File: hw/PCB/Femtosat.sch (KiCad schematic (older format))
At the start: 6 parts, among them U1 SAMD21G, U2 TRH-G2, U5 XA1110, Y1 32.768kHz

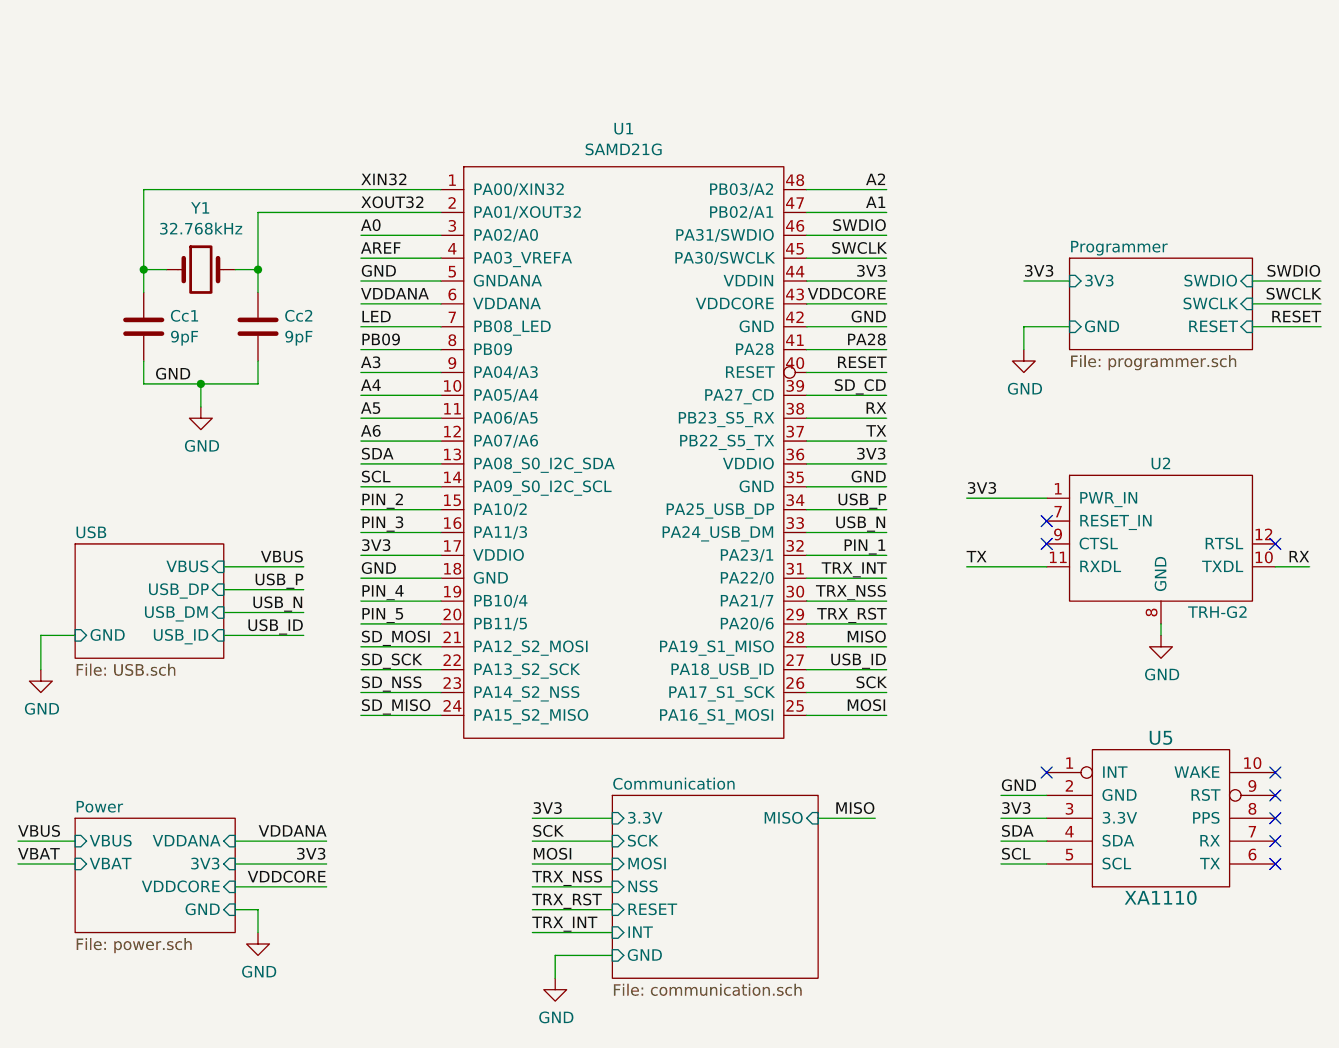
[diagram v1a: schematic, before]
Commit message: Added a footprint library for a micro SD card. Updated the schematic. Replaced the SAMD21G with the SAMD21E (32 pin variant). Added a data logger and a reset button.
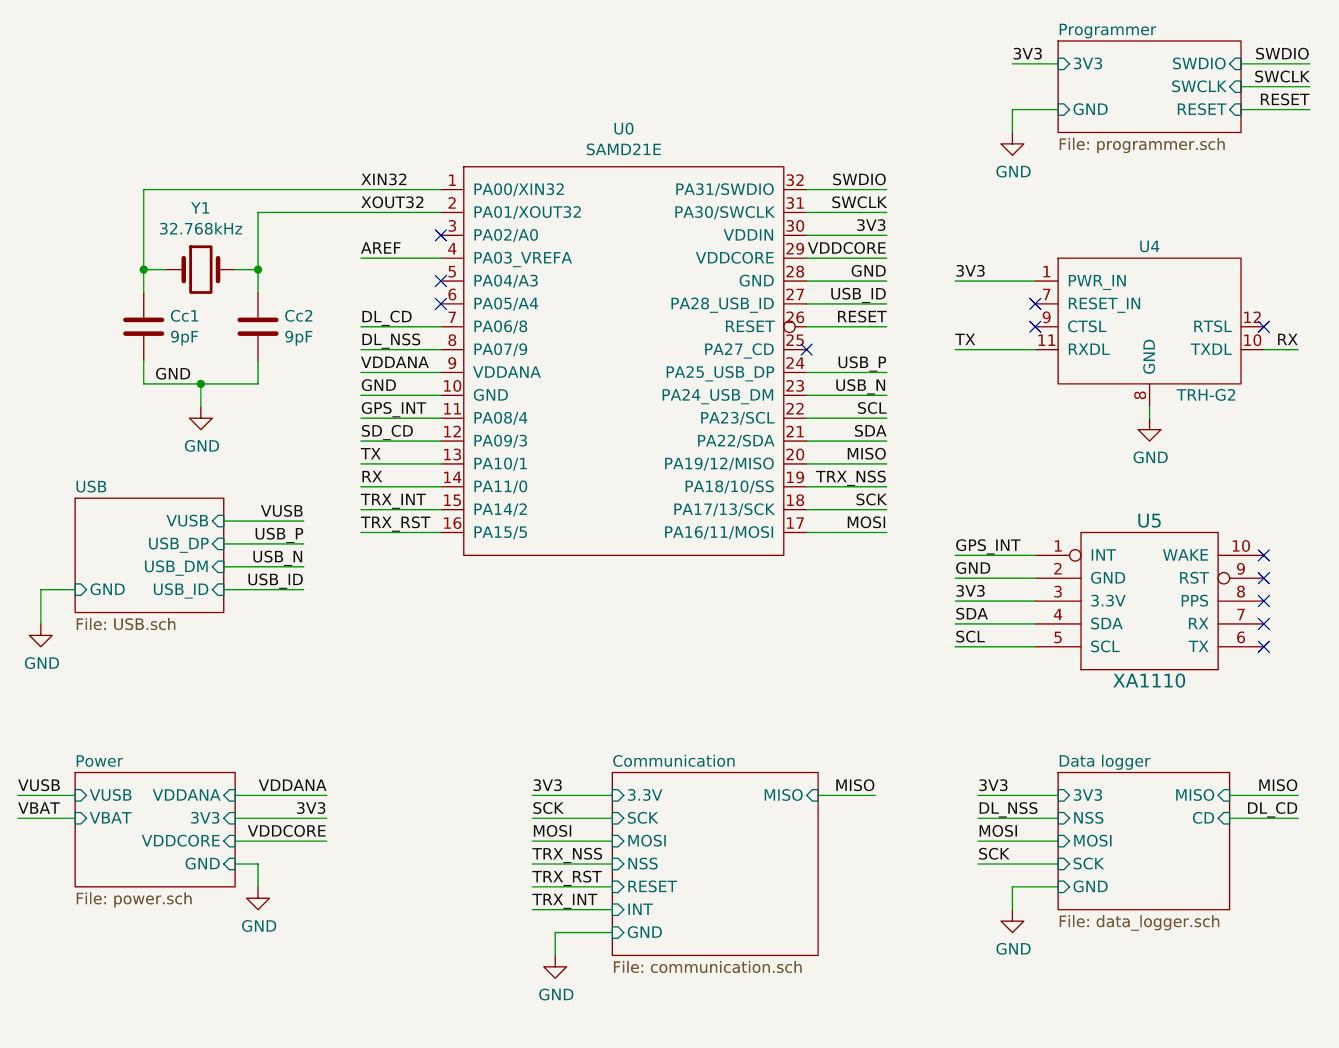
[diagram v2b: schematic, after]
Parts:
- removed U1: SAMD21G, Package_QFP:TQFP-48_7x7mm_P0.5mm, symbol Arduino:SAMD21G
- added U0: SAMD21E, symbol Arduino:SAMD21E
- renumbered U2 to U4
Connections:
- net 3V3: now also U0.30 (VDDIN)
- net AREF: now also U0.4 (PA03_VREFA)
- net GND: now also U0.10 (GND), U0.28 (GND)
- net MISO: now also U0.20 (PA19/12/MISO)
- net MOSI: now also U0.17 (PA16/11/MOSI)
- net RESET: now also U0.26 (RESET)
- net RX: now also U0.14 (PA11/0)
- net SCK: now also U0.18 (PA17/13/SCK)
- net SCL: now also U0.22 (PA23/SCL)
- net SDA: now also U0.21 (PA22/SDA)
- net SD_CD: now also U0.12 (PA09/3)
- net SWCLK: now also U0.31 (PA30/SWCLK)
- net SWDIO: now also U0.32 (PA31/SWDIO)
- net TRX_INT: now also U0.15 (PA14/2)
- net TRX_NSS: now also U0.19 (PA18/10/SS)
- net TRX_RST: now also U0.16 (PA15/5)
- net TX: now also U0.13 (PA10/1)
- net USB_ID: now also U0.27 (PA28_USB_ID)
- net USB_N: now also U0.23 (PA24_USB_DM)
- net USB_P: now also U0.24 (PA25_USB_DP)
- net VDDANA: now also U0.9 (VDDANA)
- net VDDCORE: now also U0.29 (VDDCORE)
- net XIN32: now also U0.1 (PA00/XIN32)
- net XOUT32: now also U0.2 (PA01/XOUT32)
- net GPS_INT: now reaches U5.1 (INT)
- net GPS_INT: now also U0.11 (PA08/4)
- new net DL_CD: U0.7 (PA06/8)
- new net DL_NSS: U0.8 (PA07/9)
- no-connect marks 9 -> 12
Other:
- moved on the sheet: U4, U5

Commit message: Added pullup resistor to the chip-select pin of the uSD card slot.
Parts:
- U0: footprint (none) -> Package_QFP:TQFP-32_7x7mm_P0.8mm
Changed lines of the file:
@@
 F 0 "U0" H 5200 3565 50  0000 C CNN
 F 1 "SAMD21E" H 5200 3474 50  0000 C CNN
-F 2 "" H 5200 2450 50  0001 C CNN
+F 2 "Package_QFP:TQFP-32_7x7mm_P0.8mm" H 5200 2450 50  0001 C CNN
 F 3 "" H 5200 2450 50  0001 C CNN
 	1    5200 2550
@@
 	6900 4850 6900 4950
 $Comp
-L power:GND #PWR?
+L power:GND #PWR0114
 U 1 1 5D1E4505
 P 6900 4950
-F 0 "#PWR?" H 6900 4700 50  0001 C CNN
+F 0 "#PWR0114" H 6900 4700 50  0001 C CNN
 F 1 "GND" H 6905 4777 50  0000 C CNN
 F 2 "" H 6900 4950 50  0001 C CNN

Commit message: Ended preliminary design phase.
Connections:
- net SD_CD is gone; now on net GPS_INT: U0.12 (PA09/3)
- net GPS_INT: no longer U0.11 (PA08/4)
- no-connect marks 12 -> 13
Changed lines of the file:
@@
 Text Label 6350 2400 2    50   ~ 0
 RESET
-Text Label 4050 2900 0    50   ~ 0
-SD_CD
 Text Label 6350 2600 2    50   ~ 0
 USB_P
@@
 	4050 2700 4400 2700
 Wire Wire Line
-	4400 2800 4050 2800
-Wire Wire Line
 	4050 2900 4400 2900
 Wire Wire Line
@@
 Wire Wire Line
 	6650 3800 7000 3800
-Text Label 4050 2800 0    50   ~ 0
+Text Label 4050 2900 0    50   ~ 0
 GPS_INT
 Text Label 8150 2500 2    50   ~ 0
@@
 NoConn ~ 4400 2200
 NoConn ~ 4400 2000
+NoConn ~ 4400 2800
 $EndSCHEMATC

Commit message: Changed the pin order of the pin header to connect the femto-satellite to the GPS TRH-G2. Now this connector has a battery voltage input for a future EPS board.
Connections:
- net 3V3: no longer U4.1 (PWR_IN), U4.2 (PWR_IN)
- net VBAT: now also U4.1 (PWR_IN), U4.2 (PWR_IN)
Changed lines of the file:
@@
 	8000 2500 8150 2500
 Text Label 6650 2200 0    50   ~ 0
-3V3
+VBAT
 Text Label 6650 2500 0    50   ~ 0
 TX
